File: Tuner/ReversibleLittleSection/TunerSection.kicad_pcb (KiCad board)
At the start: 2 copper layers, 100 x 100 mm, 119 parts, among them J1 Conn_01x03, J10 Conn_01x02, J11 Conn_02x05_Odd_Even, J12 Conn_01x01, J13 Conn_01x01, J14 Conn_01x01, J15 Conn_01x01, J16 Conn_01x01, J17 Conn_01x01, J18 Conn_01x01, J19 Conn_01x01, J2 Conn_01x03, J20 Conn_01x01, J21 Conn_01x01, J22 Conn_01x01, J23 Conn_01x02, J3 Conn_01x03, J4 Conn_01x03, J5 Conn_01x03, J6 Conn_01x03, J7 Conn_01x03, J8 Conn_01x02, J9 Conn_01x02, P10 Conn_01x01, P11 Conn_01x01, P12 Conn_01x01, P2 Conn_01x01, P3 Conn_01x01, P4 Conn_01x01, P5 Conn_01x01, P6 Conn_01x01, P7 Conn_01x01, P8 Conn_01x01, P9 Conn_01x01, U1 MCP23008, U2 ULN2803A

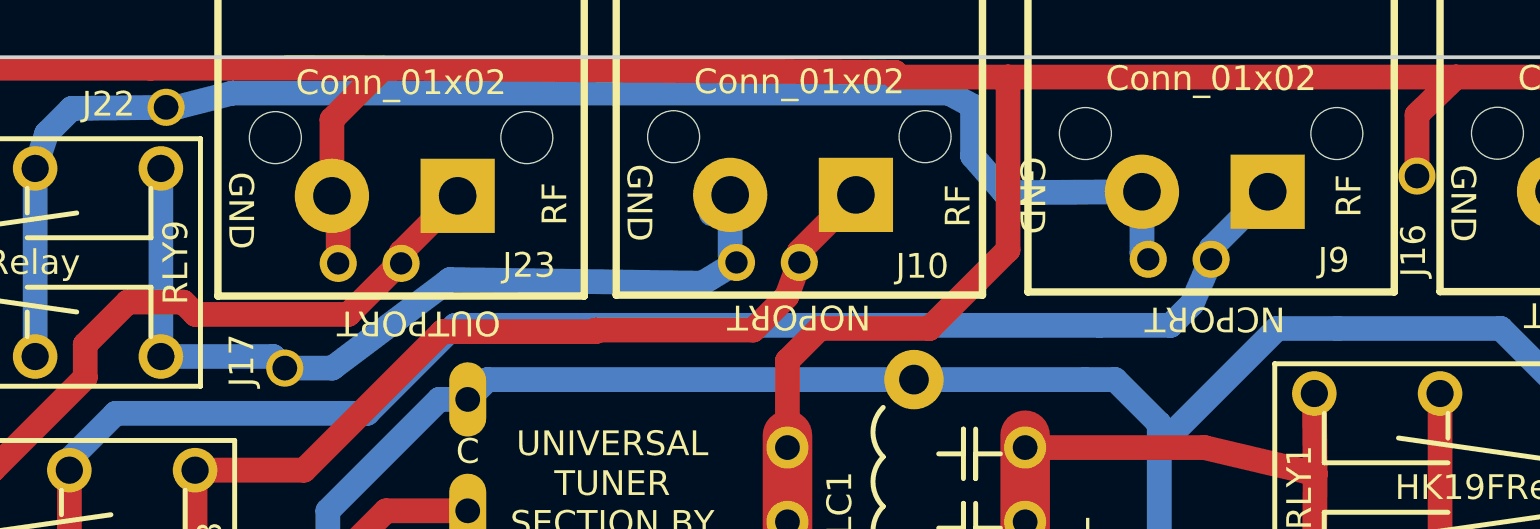
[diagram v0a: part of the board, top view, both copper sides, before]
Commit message: Change named to DirectionalCoupler, fixed order of two pins in QuadCoupler
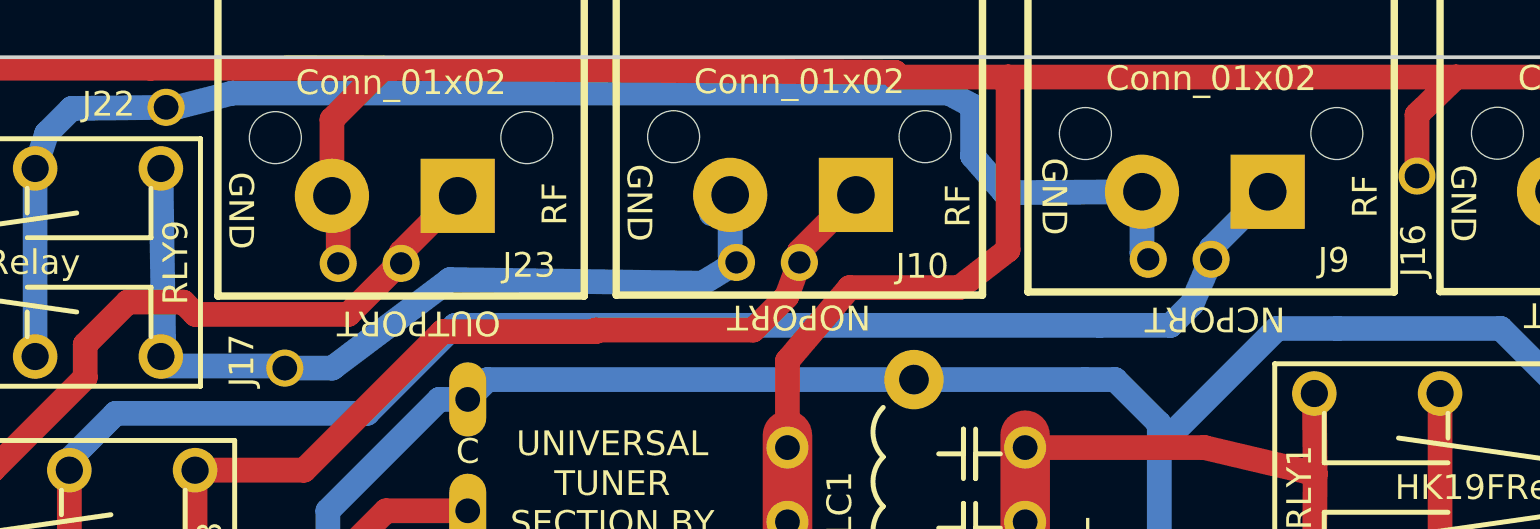
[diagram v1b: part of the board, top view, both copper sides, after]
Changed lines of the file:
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@@
     (effects (font (size 1 1) (thickness 0.15)))
   )
-  (gr_text RF (at 124.25172 55.6006 90) (layer F.SilkS)
+  (gr_text RF (at 124.9045 55.626 90) (layer F.SilkS)
     (effects (font (size 1 1) (thickness 0.15)))
   )
@@
     (effects (font (size 1 1) (thickness 0.15)))
   )
-  (gr_text GND (at 111.4425 55.5879 270) (layer F.SilkS)
+  (gr_text GND (at 112.3315 55.626 270) (layer F.SilkS)
     (effects (font (size 1 1) (thickness 0.15)))
   )
@@
   (segment (start 83.1596 52.51704) (end 85.23224 50.4444) (width 1) (layer F.Cu) (net 1))
   (segment (start 110.4773 50.8) (end 110.4773 57.785) (width 1) (layer F.Cu) (net 1))
-  (segment (start 107.3023 60.96) (end 102.87 60.96) (width 1) (layer F.Cu) (net 1))
-  (segment (start 110.4773 57.785) (end 107.3023 60.96) (width 1) (layer F.Cu) (net 1))
+  (segment (start 108.5088 59.309) (end 104.0765 59.309) (width 1) (layer F.Cu) (net 1))
+  (segment (start 110.4773 57.785) (end 108.5088 59.309) (width 1) (layer F.Cu) (net 1))
   (segment (start 132.5372 55.4228) (end 132.5372 57.8968) (width 1) (layer F.Cu) (net 1))
   (segment (start 132.5372 57.8968) (end 132.7912 58.1508) (width 1) (layer F.Cu) (net 1))
@@
   (segment (start 66.08824 62.093) (end 66.08824 54.493) (width 1) (layer F.Cu) (net 1) (status 30))
   (segment (start 101.564 65.771) (end 101.564 62.266) (width 1) (layer F.Cu) (net 1))
-  (segment (start 101.564 62.266) (end 102.87 60.96) (width 1) (layer F.Cu) (net 1))
+  (segment (start 101.564 62.266) (end 104.0765 59.309) (width 1) (layer F.Cu) (net 1))
   (segment (start 105.918 50.8) (end 105.918 50.612259) (width 1) (layer F.Cu) (net 1))
   (segment (start 85.23224 50.4444) (end 85.670853 50.4444) (width 1) (layer F.Cu) (net 1))
@@
   (segment (start 116.586 79.6925) (end 116.586 65.7225) (width 1) (layer B.Cu) (net 37))
   (segment (start 115.7285 80.55) (end 116.586 79.6925) (width 1) (layer B.Cu) (net 37))
-  (segment (start 76.24824 62.093) (end 80.7874 62.093) (width 1) (layer B.Cu) (net 38))
-  (segment (start 80.7874 62.093) (end 81.2546 62.5602) (width 1) (layer B.Cu) (net 38))
-  (segment (start 76.24824 54.493) (end 76.24824 62.093) (width 1) (layer B.Cu) (net 38))
+  (segment (start 76.37524 62.474) (end 80.9144 62.474) (width 1) (layer B.Cu) (net 38))
+  (segment (start 80.9144 62.474) (end 81.2546 62.5602) (width 1) (layer B.Cu) (net 38))
+  (segment (start 76.24824 54.493) (end 76.37524 62.474) (width 1) (layer B.Cu) (net 38))
   (segment (start 81.2546 62.5602) (end 83.17484 62.5602) (width 1) (layer B.Cu) (net 38))
   (segment (start 98.1177 59.1312) (end 99.5045 58.2905) (width 1) (layer B.Cu) (net 38) (status 20))

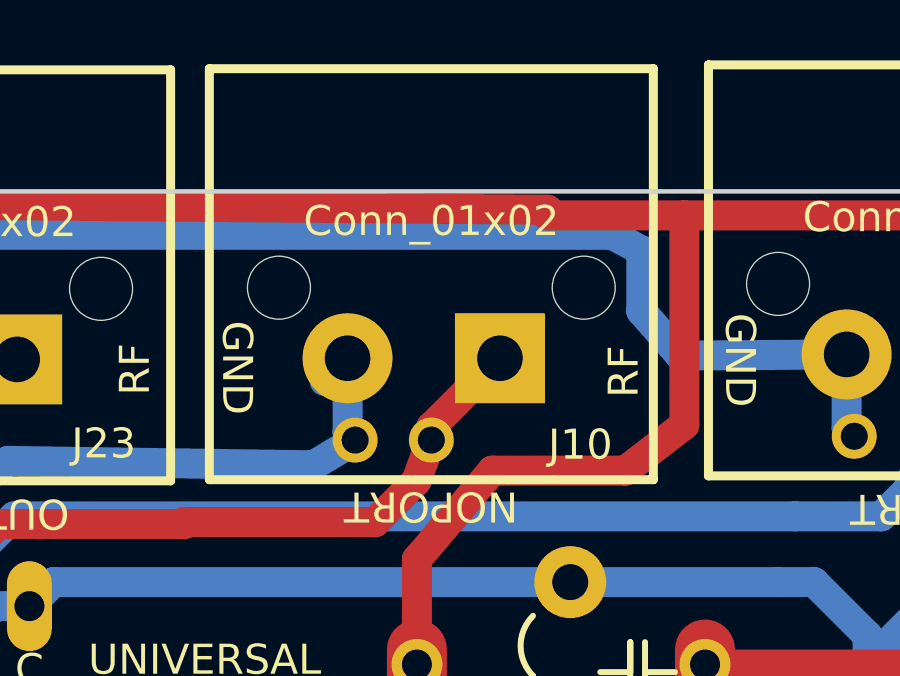
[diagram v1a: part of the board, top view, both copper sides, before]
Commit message: Some modifications to Quadcoupler for easier access
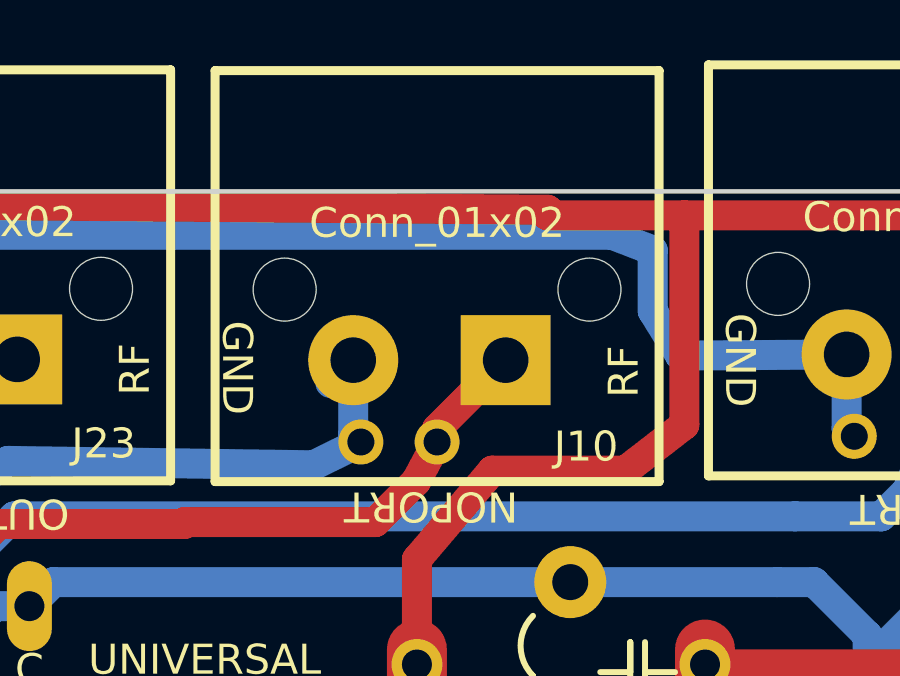
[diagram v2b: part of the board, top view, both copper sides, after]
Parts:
- moved J10 0.20 mm to (102.2, 46.0)
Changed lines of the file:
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@@
     (links 295)
     (no_connects 0)
-    (area 44.281218 45.3208 151.75012 153.921938)
+    (area 49.924999 49.924999 150.075001 150.075001)
     (thickness 1.6)
     (drawings 30)
@@
   )
   (module tuner:bnc_90_1-1337543-0_pad_combo (layer F.Cu)
-    (at 102.0445 45.9105 180)
+    (at 102.235 45.974 180)
     (descr "BNC connector, Tyco 1-1337543-0")
     (fp_text reference J10 (at -4.9657 -12.5349 180) (layer F.SilkS)
@@
   (segment (start 81.49 79.8) (end 84.455 76.835) (width 1) (layer F.Cu) (net 21))
   (segment (start 89.308 78.4495) (end 89.308 80.929) (width 1) (layer F.Cu) (net 21) (status 30))
-  (segment (start 102.0445 58.2905) (end 101.5365 59.6646) (width 1) (layer F.Cu) (net 22) (status 10))
+  (segment (start 102.235 58.354) (end 101.5365 59.6646) (width 1) (layer F.Cu) (net 22) (status 10))
   (segment (start 93.8149 61.0235) (end 93.8149 61.087) (width 1) (layer F.Cu) (net 22))
   (segment (start 100.1776 61.0235) (end 93.8149 61.0235) (width 1) (layer F.Cu) (net 22))
   (segment (start 101.5365 59.6646) (end 100.1776 61.0235) (width 1) (layer F.Cu) (net 22))
-  (segment (start 102.0445 58.2905) (end 102.0445 57.8485) (width 1) (layer F.Cu) (net 22) (status 30))
-  (segment (start 102.0445 57.8485) (end 104.3305 55.5625) (width 1) (layer F.Cu) (net 22) (status 30))
+  (segment (start 102.235 58.354) (end 102.235 57.912) (width 1) (layer F.Cu) (net 22) (status 30))
+  (segment (start 102.235 57.912) (end 104.521 55.626) (width 1) (layer F.Cu) (net 22) (status 30))
   (segment (start 77.63 66.685) (end 82.032 66.685) (width 1) (layer F.Cu) (net 22))
   (segment (start 87.63 61.087) (end 93.8149 61.087) (width 1) (layer F.Cu) (net 22))
@@
   (segment (start 76.24824 54.493) (end 76.37524 62.474) (width 1) (layer B.Cu) (net 38))
   (segment (start 81.2546 62.5602) (end 83.17484 62.5602) (width 1) (layer B.Cu) (net 38))
-  (segment (start 98.1177 59.1312) (end 99.5045 58.2905) (width 1) (layer B.Cu) (net 38) (status 20))
+  (segment (start 98.1177 59.1312) (end 99.695 58.354) (width 1) (layer B.Cu) (net 38) (status 20))
   (segment (start 87.92972 58.98388) (end 98.1177 59.1312) (width 1) (layer B.Cu) (net 38))
   (segment (start 83.17484 62.5602) (end 87.92972 58.98388) (width 1) (layer B.Cu) (net 38))
-  (segment (start 99.2505 55.5625) (end 99.2505 58.0365) (width 1) (layer B.Cu) (net 38) (status 30))
-  (segment (start 99.2505 58.0365) (end 99.5045 58.2905) (width 1) (layer B.Cu) (net 38) (status 30))
-  (segment (start 98.4885 56.3245) (end 99.2505 55.5625) (width 1) (layer B.Cu) (net 38) (status 30))
+  (segment (start 99.441 55.626) (end 99.441 58.1) (width 1) (layer B.Cu) (net 38) (status 30))
+  (segment (start 99.441 58.1) (end 99.695 58.354) (width 1) (layer B.Cu) (net 38) (status 30))
+  (segment (start 98.679 56.388) (end 99.441 55.626) (width 1) (layer B.Cu) (net 38) (status 30))
   (segment (start 116.1415 136.9695) (end 116.1415 139.2555) (width 0.35) (layer B.Cu) (net 39) (status 30))
   (segment (start 116.1415 139.2555) (end 116.078 139.319) (width 0.35) (layer B.Cu) (net 39) (status 30))
@@
   (segment (start 76.87818 52.02428) (end 79.1337 51.4477) (width 1) (layer B.Cu) (net 73) (status 10))
   (segment (start 110.3376 55.4736) (end 115.8875 55.4355) (width 1) (layer B.Cu) (net 73) (status 20))
-  (segment (start 109.0422 53.9877) (end 110.3376 55.4736) (width 1) (layer B.Cu) (net 73))
-  (segment (start 109.0422 51.9684) (end 109.0422 53.9877) (width 1) (layer B.Cu) (net 73))
-  (segment (start 108.077 51.4477) (end 109.0422 51.9684) (width 1) (layer B.Cu) (net 73))
+  (segment (start 109.4232 53.9877) (end 110.3376 55.4736) (width 1) (layer B.Cu) (net 73))
+  (segment (start 109.4232 51.9684) (end 109.4232 53.9877) (width 1) (layer B.Cu) (net 73))
+  (segment (start 108.077 51.4477) (end 109.4232 51.9684) (width 1) (layer B.Cu) (net 73))
   (segment (start 79.1337 51.4477) (end 108.077 51.4477) (width 1) (layer B.Cu) (net 73))
   (segment (start 76.45908 52.02428) (end 72.644 52.07) (width 1) (layer B.Cu) (net 73) (status 10))

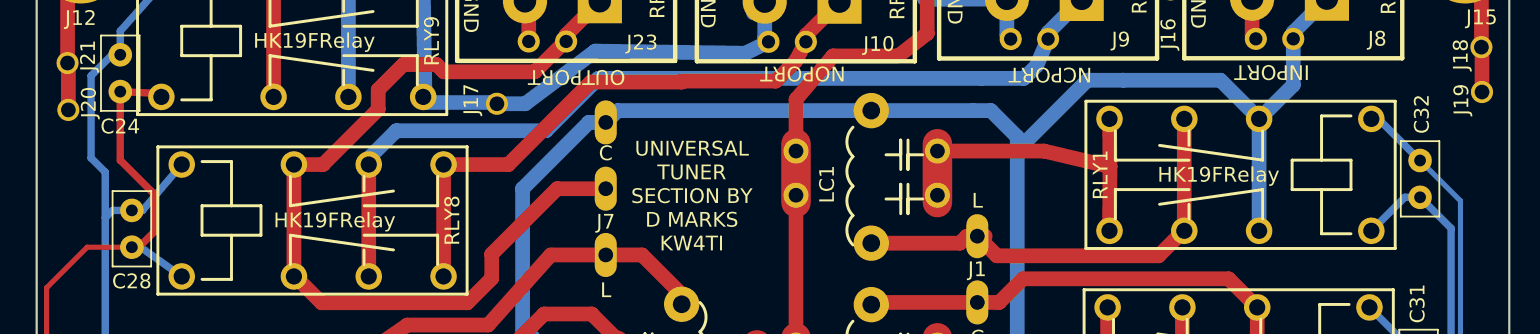
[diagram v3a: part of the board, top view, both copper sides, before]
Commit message: Added extra capacitors between relay power and ground posts
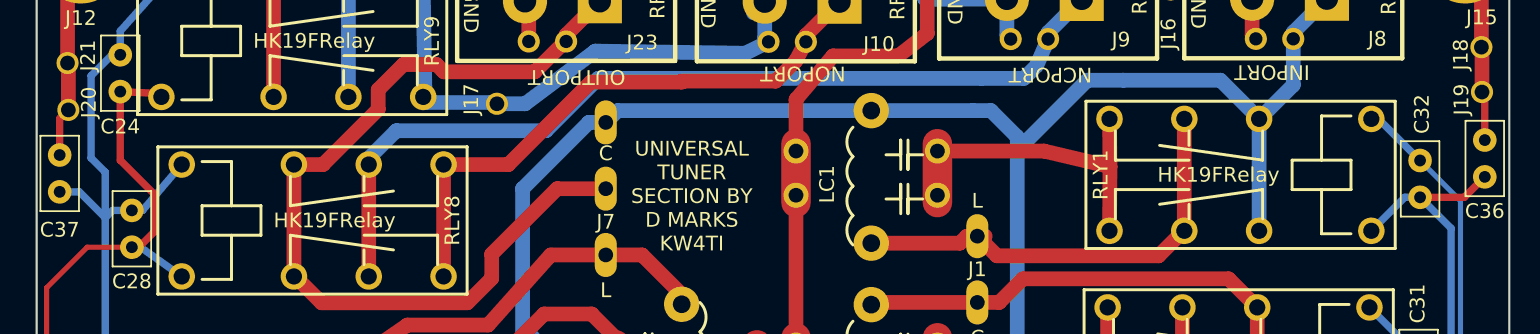
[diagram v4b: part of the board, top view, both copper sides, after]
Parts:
- added C36: 10 nF, Capacitors_THT:C_Disc_D5.0mm_W2.5mm_P2.50mm, F.Cu at (148.3, 65.0)
- added C37: 10 nF, Capacitors_THT:C_Disc_D5.0mm_W2.5mm_P2.50mm, F.Cu at (51.6, 66.0)
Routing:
- net RLYPWR: track 351.0 -> 359.8 mm
- net Net-(C36-Pad1): track 12.4 -> 15.7 mm
- net Net-(C37-Pad1): track 13.5 -> 16.8 mm

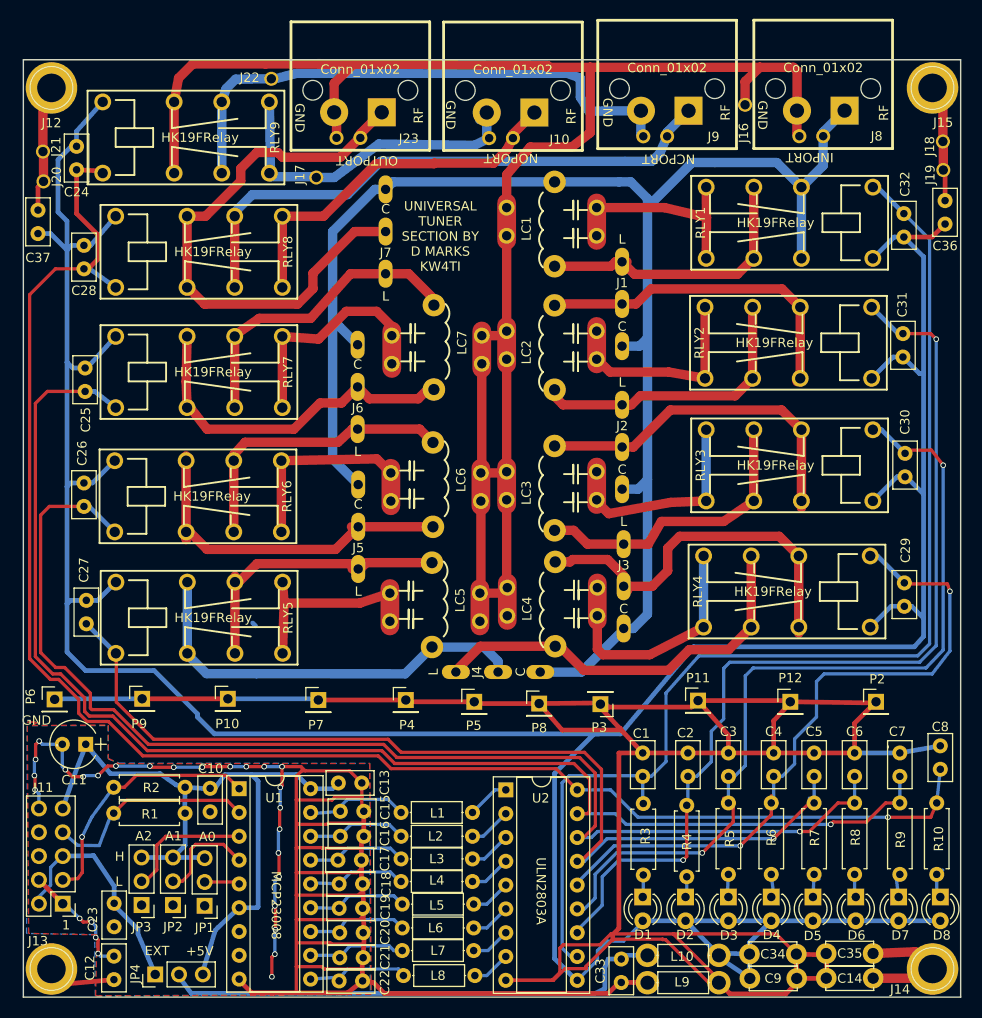
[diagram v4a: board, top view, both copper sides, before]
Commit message: Added extra mounting holes to ground ReversibleLittleSection
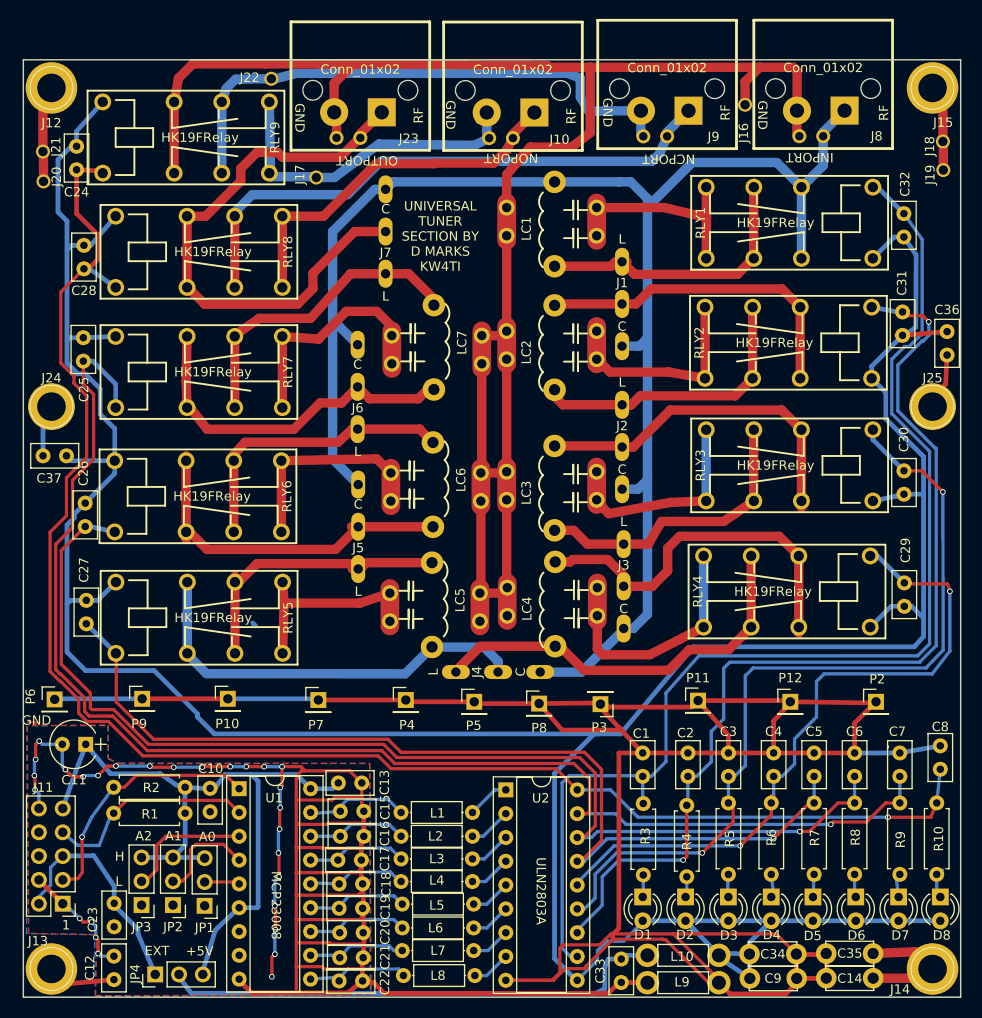
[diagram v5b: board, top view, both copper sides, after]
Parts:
- added J24: Conn_01x01, Connectors:1pin, F.Cu at (53.0, 87.0)
- added J25: Conn_01x01, Connectors:1pin, F.Cu at (147.0, 87.0)
- moved C37 26.2 mm to (52.1, 92.2), turned to 0 degrees
- moved C36 16.5 mm to (148.6, 81.5), turned to 90 degrees
- moved C25 3.24 mm to (56.4, 79.7)
- moved C31 2.31 mm to (143.8, 79.4)
- moved C26 2.16 mm to (56.6, 97.3)
- moved C30 1.87 mm to (143.9, 96.3)
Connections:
- J12 pad 1: Net-(C37-Pad1) -> Net-(J12-Pad1)
- J15 pad 1: Net-(C36-Pad1) -> Net-(J15-Pad1)
- J18 pad 1: Net-(C36-Pad1) -> Net-(J15-Pad1)
- J19 pad 1: Net-(C36-Pad1) -> Net-(J15-Pad1)
- J20 pad 1: Net-(C37-Pad1) -> Net-(J12-Pad1)
- J21 pad 1: Net-(C37-Pad1) -> Net-(J12-Pad1)
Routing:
- net Net-(J12-Pad1): track 0.00 -> 13.5 mm
- net Net-(J15-Pad1): track 0.00 -> 12.7 mm
- net Net-(C37-Pad1): track 16.8 -> 5.62 mm
- net Net-(C36-Pad1): track 15.7 -> 5.08 mm
- net RLY6: track 131.5 -> 123.7 mm
- net RLYPWR: track 359.8 -> 353.7 mm
- net RLY2: track 103.9 -> 107.2 mm
- net RLY1: track 124.2 -> 126.9 mm
- net RLY7: track 146.4 -> 149.0 mm
- net RLY8: track 175.3 -> 173.6 mm
- net RLY3: track 91.6 -> 90.6 mm
